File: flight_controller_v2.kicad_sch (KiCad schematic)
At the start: 0 parts

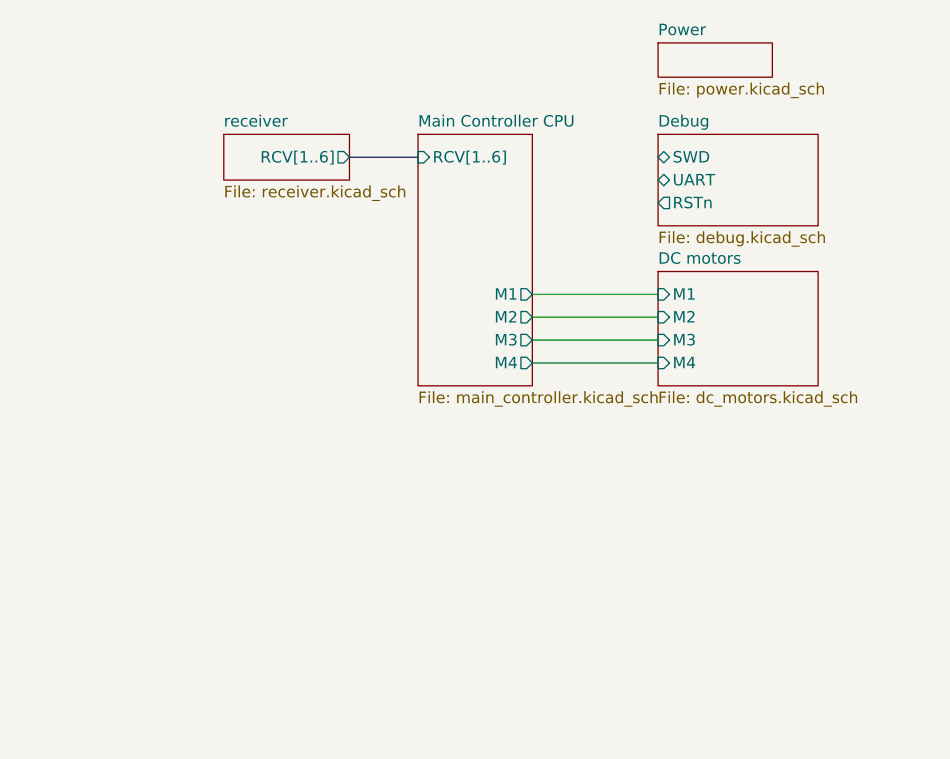
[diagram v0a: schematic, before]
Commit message: Initial schematic version
This is now a clean and ready version of the schematic:
That means:
- Schematic has been reviewed,
- It's fully annotated,
- All elements have been checked for availability with JLCPCB,
- Footprints were assigned,
- ERC is green.

No design changes should be added for this version until
the PCB is present and version is released.
Only bugfixes are possible now.
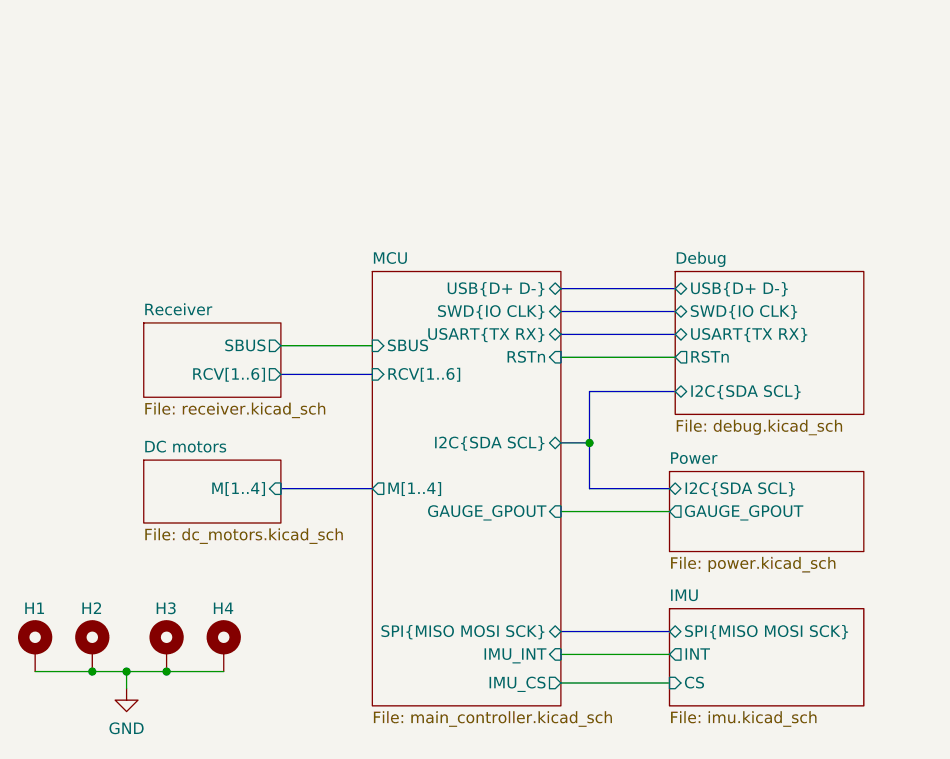
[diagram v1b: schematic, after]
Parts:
- added H1, H2, H3, H4: MountingHole_Pad, MountingHole:MountingHole_2.2mm_M2_Pad, symbol Mechanical:MountingHole_Pad
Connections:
- new net GND: H1.1, H2.1, H3.1, H4.1
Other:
- sheet Main Controller CPU renamed MCU
- sheet receiver renamed Receiver
- added sheet IMU (imu.kicad_sch)
- sheet DC motors ports: added M[1..4]; removed M1, M2, M3, M4
- sheet Debug ports: added I2C{SDA SCL}, SWD{IO CLK}, USART{TX RX}, USB{D+ D-}; removed SWD, UART
- sheet MCU ports: added GAUGE_GPOUT, I2C{SDA SCL}, IMU_CS, IMU_INT, M[1..4], RSTn, SBUS, SPI{MISO MOSI SCK}, SWD{IO CLK}, USART{TX RX}, USB{D+ D-}; removed M1, M2, M3, M4
- sheet Power ports: added GAUGE_GPOUT, I2C{SDA SCL}; removed none
- sheet Receiver ports: added SBUS; removed none
